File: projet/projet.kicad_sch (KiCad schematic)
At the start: 17 parts, among them J301 EMB_P3.81_1x02_VERTICAL, J302 EMB_P3.81_1x04_VERTICAL, Q301 MOS P 20V 2A, U301 Raspberry-Pi-Pico_Linked

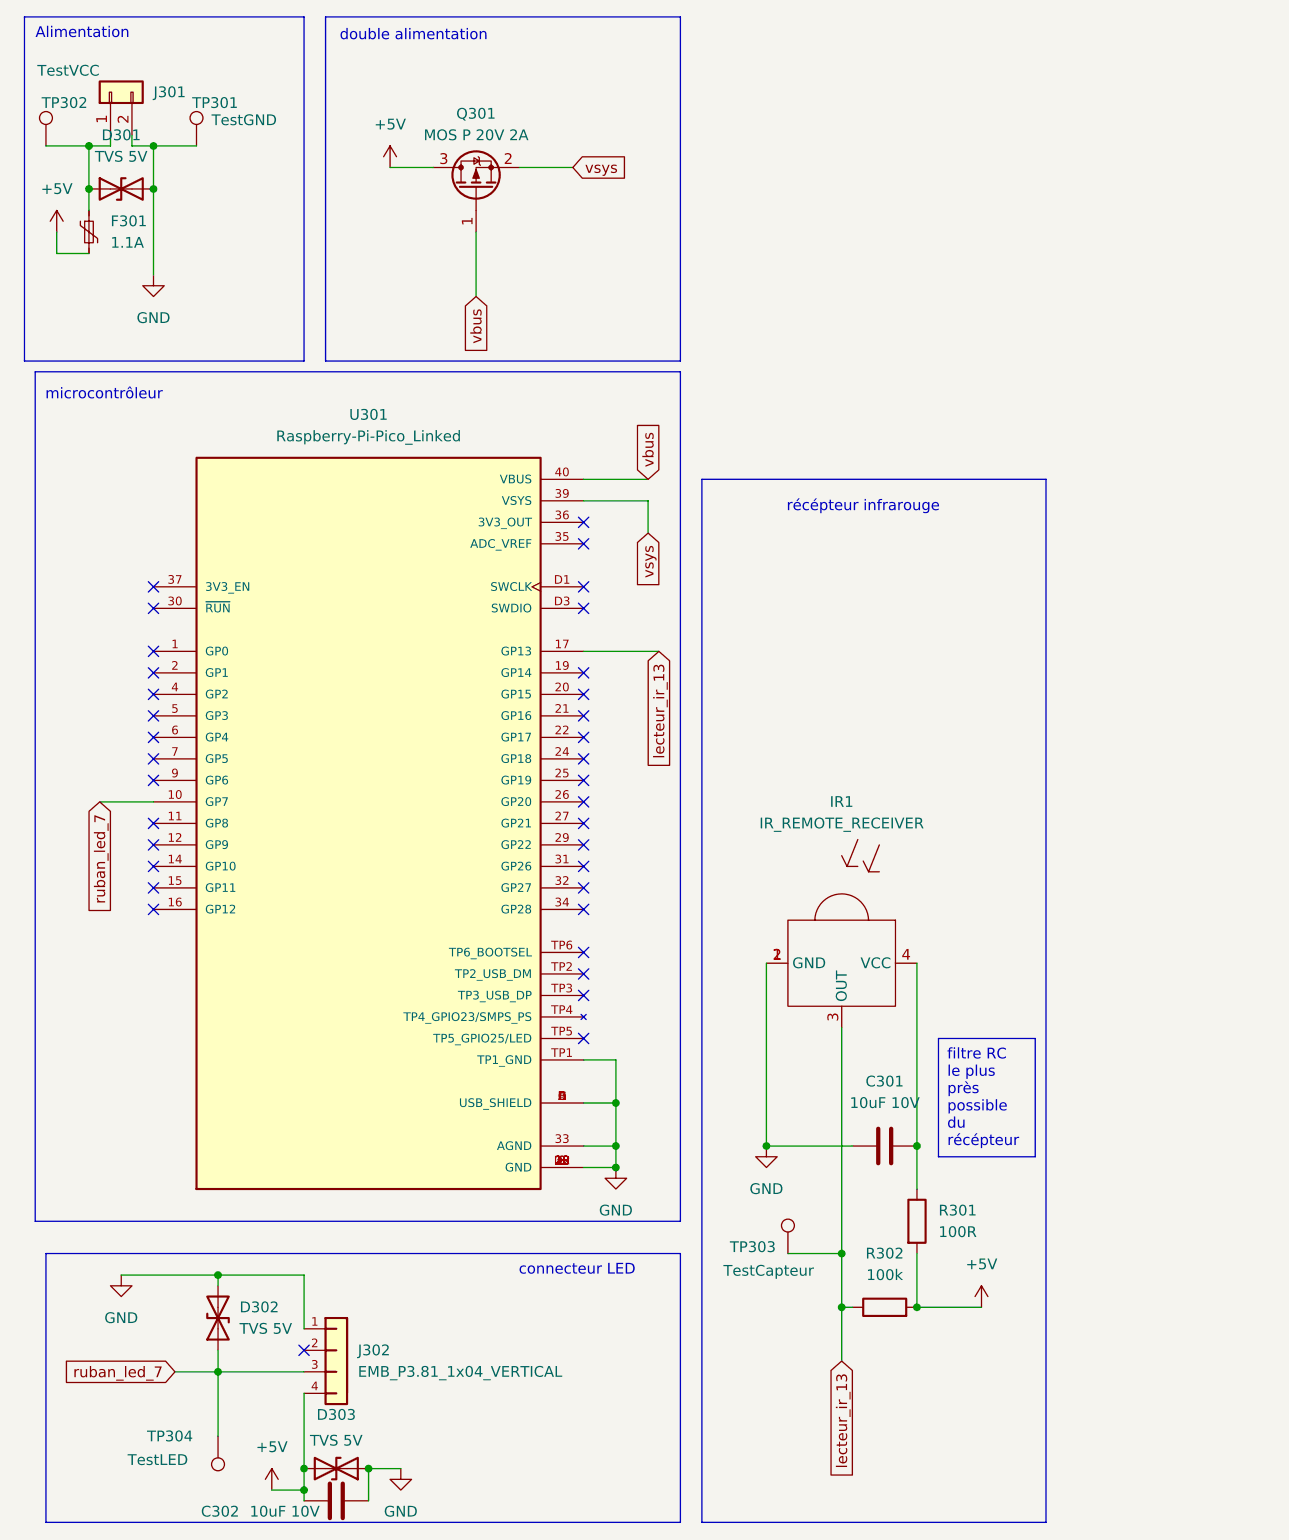
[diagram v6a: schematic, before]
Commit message: Ajout de graphisme et fichiers de fabrications
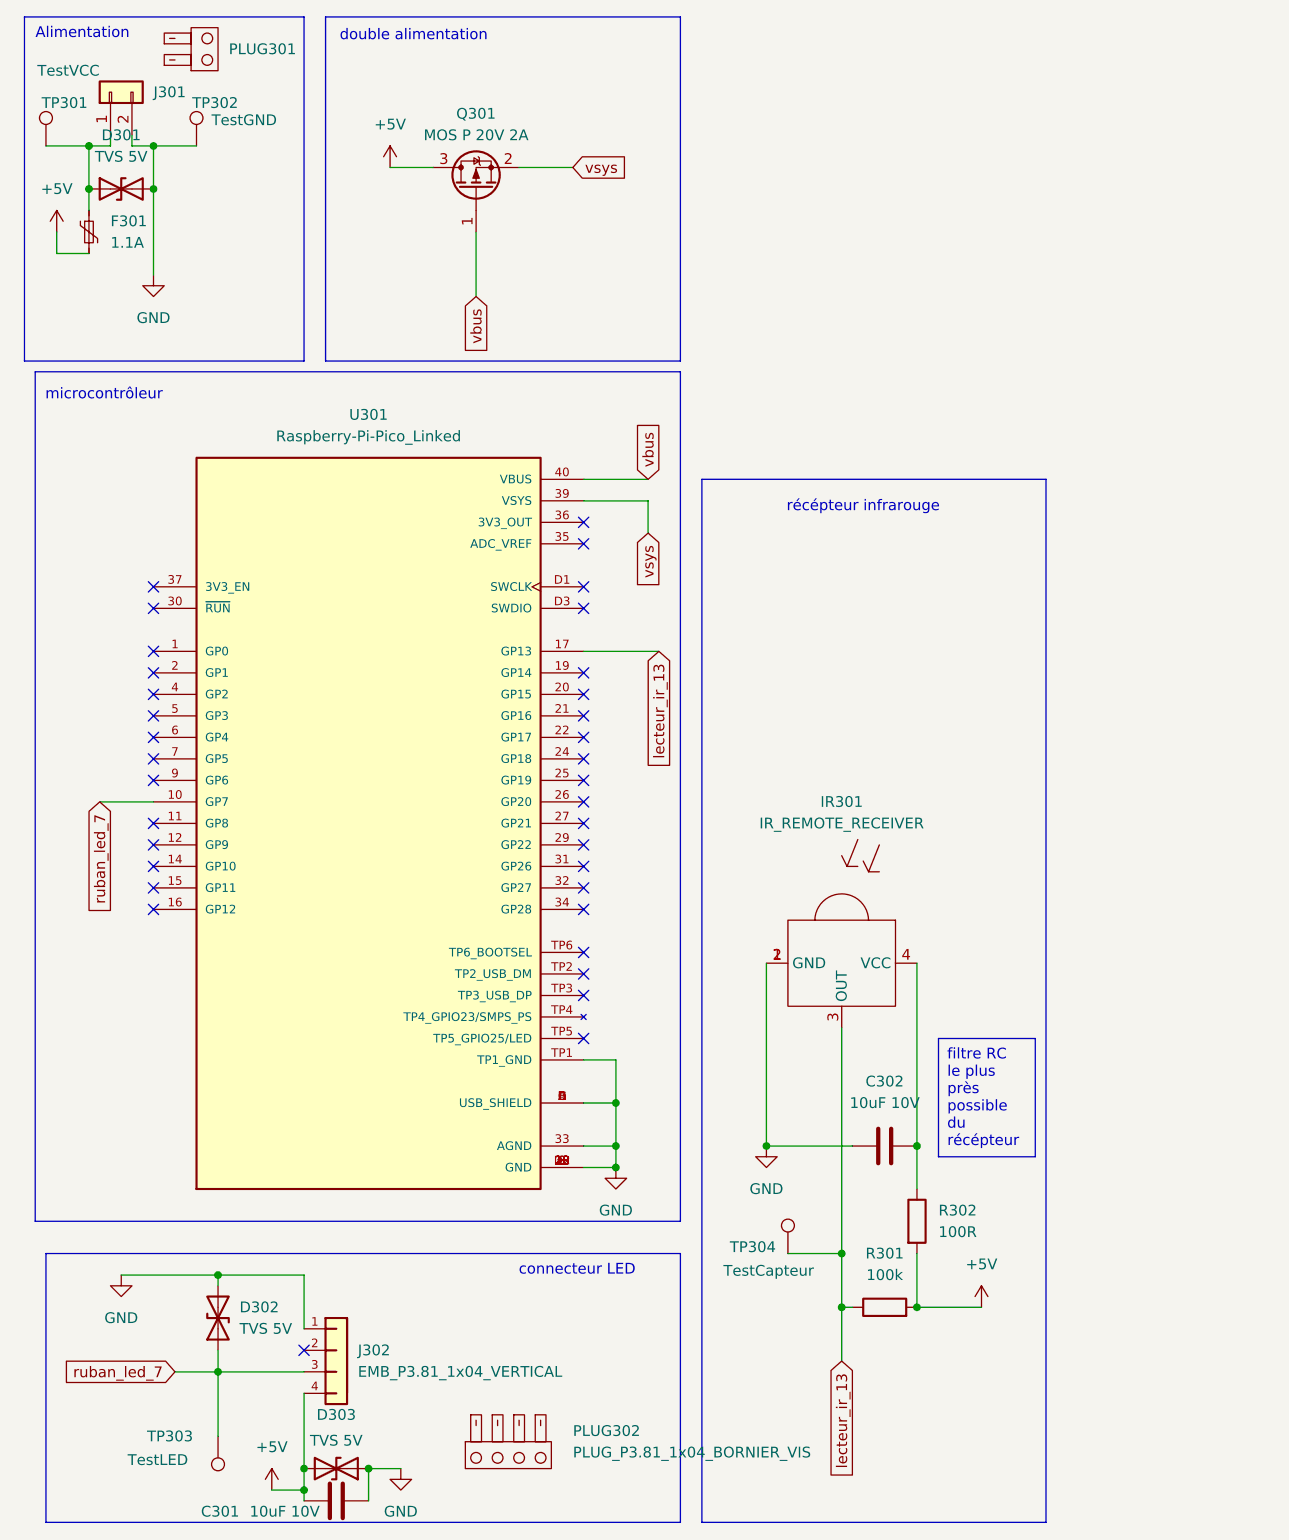
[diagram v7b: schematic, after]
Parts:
- added PLUG301: PLUG_P3.81_1x02_BORNIER_VIS, symbol codium_Connectors:PLUG_P3.81_1x02_BORNIER_VIS
- added PLUG302: PLUG_P3.81_1x04_BORNIER_VIS, symbol codium_Connectors:PLUG_P3.81_1x04_BORNIER_VIS
- renumbered C302 to C301, C301 to C302, IR1 to IR301, R302 to R301, R301 to R302, TP302 to TP301, TP301 to TP302, TP304 to TP303, TP303 to TP304
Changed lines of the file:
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@@
 		(on_board yes)
 		(dnp no)
-		(property "Reference" "TP303"
+		(property "Reference" "TP304"
 			(at 97.282 159.258 0)
 			(effects
@@
 			(project ""
 				(path "/a8729fd7-f378-4132-940e-1f2a87480560"
-					(reference "TP303")
+					(reference "TP304")
 					(unit 1)
 				)
@@
 		(dnp no)
 		(fields_autoplaced yes)
-		(property "Reference" "#PWR0302"
+		(property "Reference" "#PWR0309"
 			(at 127 170.18 0)
 			(effects
@@
 			(project ""
 				(path "/a8729fd7-f378-4132-940e-1f2a87480560"
-					(reference "#PWR0302")
+					(reference "#PWR0309")
 					(unit 1)
 				)
@@
 		(dnp no)
 		(fields_autoplaced yes)
-		(property "Reference" "R302"
+		(property "Reference" "R301"
 			(at 115.57 160.02 90)
 			(effects
@@
 			(project ""
 				(path "/a8729fd7-f378-4132-940e-1f2a87480560"
-					(reference "R302")
+					(reference "R301")
 					(unit 1)
 				)
@@
 		(dnp no)
 		(fields_autoplaced yes)
-		(property "Reference" "R301"
+		(property "Reference" "R302"
 			(at 121.92 154.9399 0)
 			(effects
@@
 			(project ""
 				(path "/a8729fd7-f378-4132-940e-1f2a87480560"
-					(reference "R301")
+					(reference "R302")
 					(unit 1)
 				)
@@
 		(dnp no)
 		(fields_autoplaced yes)
-		(property "Reference" "IR1"
+		(property "Reference" "IR301"
 			(at 110.49 106.68 90)
 			(effects
@@
 			(project ""
 				(path "/a8729fd7-f378-4132-940e-1f2a87480560"
-					(reference "IR1")
+					(reference "IR301")
 					(unit 1)
 				)
@@
 		(dnp no)
 		(fields_autoplaced yes)
-		(property "Reference" "#PWR0308"
+		(property "Reference" "#PWR0302"
 			(at 25.4 168.91 0)
 			(effects
@@
 			(project ""
 				(path "/a8729fd7-f378-4132-940e-1f2a87480560"
-					(reference "#PWR0308")
+					(reference "#PWR0302")
 					(unit 1)
 				)
@@
 		(dnp no)
 		(fields_autoplaced yes)
-		(property "Reference" "#PWR0303"
+		(property "Reference" "#PWR0305"
 			(at 57.15 35.56 0)
 			(effects
@@
 			(project "projet"
 				(path "/a8729fd7-f378-4132-940e-1f2a87480560"
-					(reference "#PWR0303")
+					(reference "#PWR0305")
 					(unit 1)
 				)
@@
 		(dnp no)
 		(fields_autoplaced yes)
-		(property "Reference" "C301"
+		(property "Reference" "C302"
 			(at 115.57 139.7 90)
 			(effects
@@
 			(project ""
 				(path "/a8729fd7-f378-4132-940e-1f2a87480560"
-					(reference "C301")
+					(reference "C302")
 					(unit 1)
 				)
@@
 		(on_board yes)
 		(dnp no)
-		(property "Reference" "C302"
+		(property "Reference" "C301"
 			(at 37.084 190.5 90)
 			(effects
@@
 			(project "projet"
 				(path "/a8729fd7-f378-4132-940e-1f2a87480560"
-					(reference "C302")
+					(reference "C301")
 					(unit 1)
 				)
@@
 		(dnp no)
 		(fields_autoplaced yes)
-		(property "Reference" "#PWR0305"
+		(property "Reference" "#PWR0303"
 			(at 29.21 50.8 0)
 			(effects
@@
 			(project ""
 				(path "/a8729fd7-f378-4132-940e-1f2a87480560"
-					(reference "#PWR0305")
+					(reference "#PWR0303")
 					(unit 1)
 				)
@@
 		(dnp no)
 		(fields_autoplaced yes)
-		(property "Reference" "#PWR0301"
+		(property "Reference" "#PWR0308"
 			(at 101.6 153.67 0)
 			(effects
@@
 			(project ""
 				(path "/a8729fd7-f378-4132-940e-1f2a87480560"
-					(reference "#PWR0301")
+					(reference "#PWR0308")
 					(unit 1)
 				)
@@
 		(on_board yes)
 		(dnp no)
-		(property "Reference" "TP302"
+		(property "Reference" "TP301"
 			(at 16.002 24.13 0)
 			(effects
@@
 			(project ""
 				(path "/a8729fd7-f378-4132-940e-1f2a87480560"
-					(reference "TP302")
+					(reference "TP301")
+					(unit 1)
+				)
+			)
+		)
+	)
+	(symbol
+		(lib_id "codium_Connectors:PLUG_P3.81_1x02_BORNIER_VIS")
+		(at 34.29 17.78 90)
+		(unit 1)
+		(exclude_from_sim no)
+		(in_bom yes)
+		(on_board no)
+		(dnp no)
+		(fields_autoplaced yes)
+		(property "Reference" "PLUG301"
+			(at 38.1 17.7799 90)
+			(effects
+				(font
+					(size 1.27 1.27)
+				)
+				(justify right)
+			)
+		)
+		(property "Value" "PLUG_P3.81_1x02_BORNIER_VIS"
+			(at 27.178 21.082 0)
+			(effects
+				(font
+					(size 1.27 1.27)
+				)
+				(hide yes)
+			)
+		)
+		(property "Footprint" ""
+			(at 34.29 17.78 0)
+			(effects
+				(font
+					(size 1.27 1.27)
+				)
+				(hide yes)
+			)
+		)
+		(property "Datasheet" "${CODIUM_DOC_DIR}\\Connectors\\Plug_Ningbo-Kangnex-Elec-BORNIER_VIS.pdf"
+			(at 27.178 13.462 0)
+			(effects
+				(font
+					(size 1.27 1.27)
+				)
+				(hide yes)
+			)
+		)
+		(property "Description" "Fiche bornier débrochable à vis Générique"
+			(at 27.178 16.002 0)
+			(effects
+				(font
+					(size 1.27 1.27)
+				)
+				(hide yes)
+			)
+		)
+		(property "MAN" "Ningbo Kangnex Elec "
+			(at 27.178 13.462 0)
+			(effects
+				(font
+					(size 1.27 1.27)
+				)
+				(hide yes)
+			)
+		)
+		(property "MPN" "WJ15EDGK-3.81-2P"
+			(at 27.178 13.462 0)
+			(effects
+				(font
+					(size 1.27 1.27)
+				)
+				(hide yes)
+			)
+		)
+		(property "IPN" "PLUG_P3.81_1x02_BORNIER_VIS"
+			(at 34.29 17.78 0)
+			(effects
+				(font
+					(size 1.27 1.27)
+				)
+				(hide yes)
+			)
+		)
+		(instances
+			(project ""
+				(path "/a8729fd7-f378-4132-940e-1f2a87480560"
+					(reference "PLUG301")
 					(unit 1)
 				)
@@
 		(dnp no)
 		(fields_autoplaced yes)
-		(property "Reference" "#PWR0314"
+		(property "Reference" "#PWR0307"
 			(at 83.82 156.21 0)
 			(effects
@@
 			(project ""
 				(path "/a8729fd7-f378-4132-940e-1f2a87480560"
-					(reference "#PWR0314")
+					(reference "#PWR0307")
 					(unit 1)
 				)
@@
 		(dnp no)
 		(fields_autoplaced yes)
-		(property "Reference" "#PWR0316"
+		(property "Reference" "#PWR0306"
 			(at 58.42 191.77 0)
 			(effects
@@
 			(project "projet"
 				(path "/a8729fd7-f378-4132-940e-1f2a87480560"
-					(reference "#PWR0316")
+					(reference "#PWR0306")
 					(unit 1)
 				)
@@
 		(dnp no)
 		(fields_autoplaced yes)
-		(property "Reference" "#PWR0307"
+		(property "Reference" "#PWR0304"
 			(at 43.18 191.77 0)
 			(effects
@@
 			(project ""
 				(path "/a8729fd7-f378-4132-940e-1f2a87480560"
-					(reference "#PWR0307")
+					(reference "#PWR0304")
 					(unit 1)
 				)
@@
 		(on_board yes)
 		(dnp no)
-		(property "Reference" "TP304"
+		(property "Reference" "TP303"
 			(at 28.448 181.61 0)
 			(effects
@@
 			(project ""
 				(path "/a8729fd7-f378-4132-940e-1f2a87480560"
-					(reference "TP304")
+					(reference "TP303")
+					(unit 1)
+				)
+			)
+		)
+	)
+	(symbol
+		(lib_id "codium_Connectors:PLUG_P3.81_1x04_BORNIER_VIS")
+		(at 71.12 182.88 0)
+		(unit 1)
+		(exclude_from_sim no)
+		(in_bom yes)
+		(on_board no)
+		(dnp no)
+		(fields_autoplaced yes)
+		(property "Reference" "PLUG302"
+			(at 78.74 180.9749 0)
+			(effects
+				(font
+					(size 1.27 1.27)
+				)
+				(justify left)
+			)
+		)
+		(property "Value" "PLUG_P3.81_1x04_BORNIER_VIS"
+			(at 77.47 183.515 90)
+			(effects
+				(font
+					(size 1.27 1.27)
+				)
+				(hide yes)
+			)
+		)
+		(property "Footprint" ""
+			(at 71.12 182.88 0)
+			(effects
+				(font
+					(size 1.27 1.27)
+				)
+				(hide yes)
+			)
+		)
+		(property "Datasheet" "${CODIUM_DOC_DIR}\\Connectors\\Plug_Ningbo-Kangnex-Elec-BORNIER_VIS.pdf"
+			(at 71.12 182.88 0)
+			(effects
+				(font
+					(size 1.27 1.27)
+				)
+				(hide yes)
+			)
+		)
+		(property "Description" "Fiche bornier débrochable à vis Générique"
+			(at 71.12 182.88 0)
+			(effects
+				(font
+					(size 1.27 1.27)
+				)
+				(hide yes)
+			)
+		)
+		(property "MAN" "Ningbo Kangnex Elec "
+			(at 71.12 182.88 0)
+			(effects
+				(font
+					(size 1.27 1.27)
+				)
+				(hide yes)
+			)
+		)
+		(property "MPN" "WJ15EDGK-3.81-4P"
+			(at 71.12 182.88 0)
+			(effects
+				(font
+					(size 1.27 1.27)
+				)
+				(hide yes)
+			)
+		)
+		(property "IPN" "PLUG_P3.81_1x04_BORNIER_VIS"
+			(at 78.74 183.5149 0)
+			(effects
+				(font
+					(size 1.27 1.27)
+				)
+				(justify left)
+			)
+		)
+		(instances
+			(project ""
+				(path "/a8729fd7-f378-4132-940e-1f2a87480560"
+					(reference "PLUG302")
 					(unit 1)
 				)
@@
 		(dnp no)
 		(fields_autoplaced yes)
-		(property "Reference" "#PWR0306"
+		(property "Reference" "#PWR0301"
 			(at 17.78 43.18 0)
 			(effects
@@
 			(project ""
 				(path "/a8729fd7-f378-4132-940e-1f2a87480560"
-					(reference "#PWR0306")
+					(reference "#PWR0301")
 					(unit 1)
 				)
@@
 		(on_board yes)
 		(dnp no)
-		(property "Reference" "TP301"
+		(property "Reference" "TP302"
 			(at 33.782 24.13 0)
 			(effects
@@
 			(project "projet"
 				(path "/a8729fd7-f378-4132-940e-1f2a87480560"
-					(reference "TP301")
-					(unit 1)
-				)
+					(reference "TP302")
+					(unit 1)
+				)

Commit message: Dernière modifs avant vérif externes
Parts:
- added D304, D305, D306, D307: LED GREEN, codium_Leds:LED0805, symbol codium_Leds:LED_0805_Green
- added R303, R304, R305, R306: 330R, codium_Basics:R0603, symbol codium_Resistors:R_0603_330R
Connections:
- net +5V: now also D304.2 (A)
- net GND: now also R303.2, R304.2, R305.2, R306.2
- net LED_0: now reaches U301.24 (GP18)
- net LED_0: now also D305.2 (A)
- net LED_1: now reaches U301.25 (GP19)
- net LED_1: now also D306.2 (A)
- net LED_2: now reaches U301.26 (GP20)
- net LED_2: now also D307.2 (A)
- new net: D304.1 (K), R303.1
- new net: D306.1 (K), R305.1
- new net: D305.1 (K), R304.1
- new net: D307.1 (K), R306.1
- no-connect marks 35 -> 32
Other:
- note added: "Module LED commandées"
- moved on the sheet: C302, IR301, R301, R302, TP304
